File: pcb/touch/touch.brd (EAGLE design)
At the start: 97.8 x 36.2 mm, 22 parts, among them U1 MPR084EJ

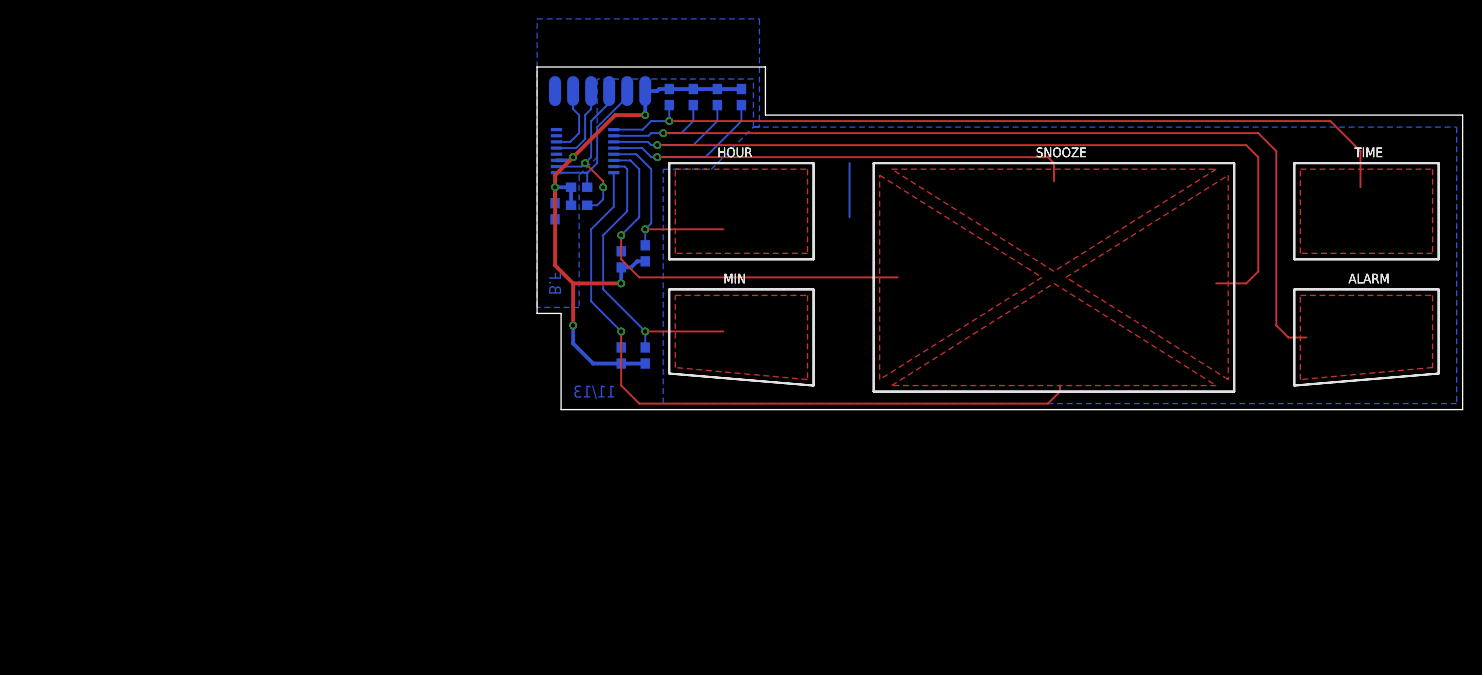
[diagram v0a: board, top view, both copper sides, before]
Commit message: Corrected drawings of touch panel PCB
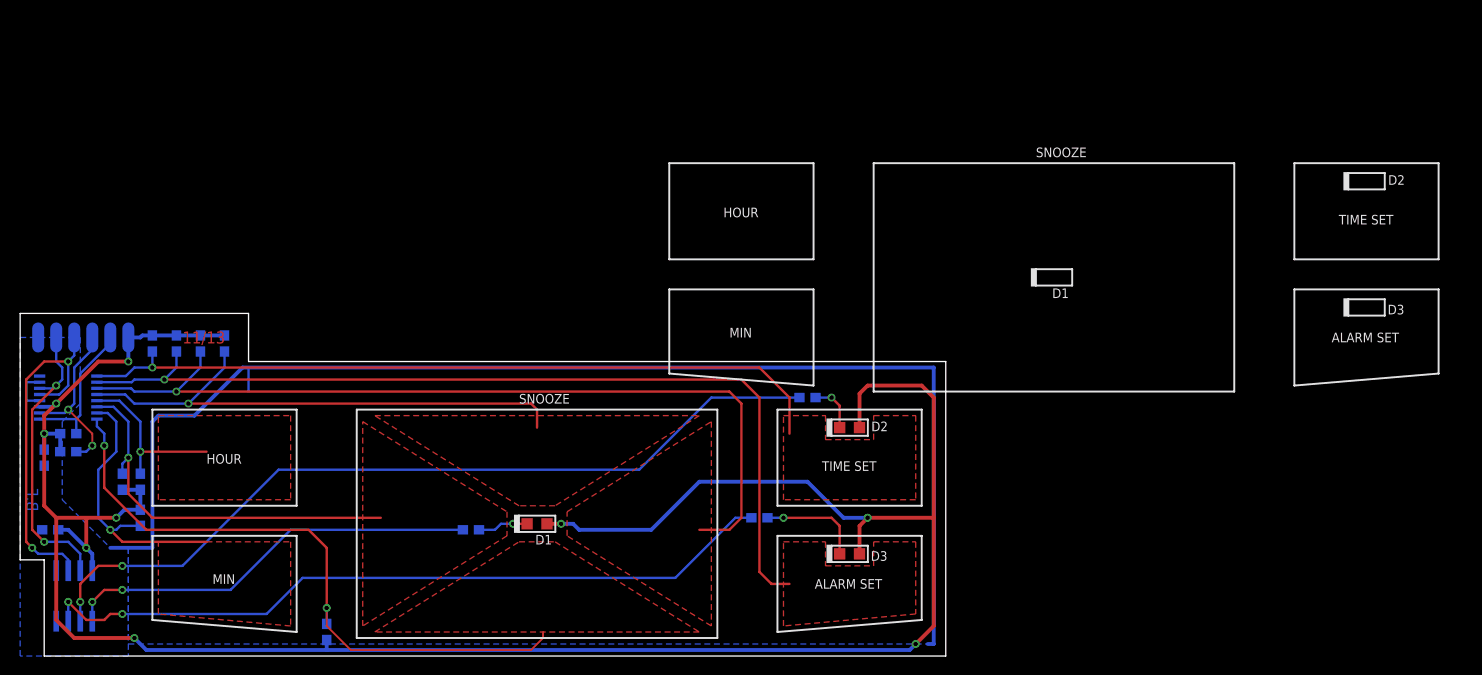
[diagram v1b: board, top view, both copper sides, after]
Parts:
- added C2: 100nF, Passive:SMD_0603
- added D1, D2, D3: {ATTR:COLOR}, Optoelectronic:CHIPLED_0805
- added R11, R12, R13: 56, Passive:SMD_0603
- added U$11, U$12, U$13, U$14, U$15, U$16: (no value), Symbols:LEGEND_ROW_30
- added U2: PCA9533D/01, IC:SOIC8
- moved !ATTN 60.5 mm to (-45.1, 7.62)
- moved !IRQ 60.5 mm to (-47.0, 7.62)
- moved 3.3V 60.5 mm to (-43.2, 7.62)
- moved R3 60.5 mm to (-35.6, 6.99)
- moved R4 60.5 mm to (-38.1, 6.99)
- moved R5 60.5 mm to (-40.6, 6.99)
- moved R7 60.5 mm to (-33.0, 6.99)
- moved SCL 60.5 mm to (-48.9, 7.62)
- moved SDA 60.5 mm to (-50.8, 7.62)
- moved U$3 60.5 mm to (-38.1, -21.0)
- moved U1 60.5 mm to (-49.5, 1.27)
- moved W6 60.5 mm to (-52.7, 7.62)
- moved C1 59.9 mm to (-52.1, -5.08)
- moved R10 59.9 mm to (-49.5, -4.45)
- moved R9 59.9 mm to (-49.5, -2.54)
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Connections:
- new net N$1: D1.K, R11.2
- new net N$2: D2.K, R12.2
- new net N$3: D3.K, R13.2
- new net N$4: R11.1, U2.1
- new net N$5: R12.1, U2.2
- new net N$6: R13.1, U2.3
- net 3.3V: now also C2.1, D1.A, D2.A, D3.A, U2.8
- net GND: now also C2.2, U2.4
- net SCL: now also U2.6
- net SDA: now also U2.7
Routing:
- net 3.3V: track 68.8 -> 257.7 mm, vias 5 -> 9
- net GND: track 5.71 -> 139.9 mm
- net N$5: track 0.00 -> 88.1 mm, vias 0 -> 2
- net N$6: track 0.00 -> 79.5 mm, vias 0 -> 2
- net N$4: track 0.00 -> 44.3 mm, vias 0 -> 2
- net SCL: track 8.76 -> 37.5 mm, vias 0 -> 2
- net SDA: track 7.48 -> 31.7 mm, vias 0 -> 2
- net N$3: track 0.00 -> 10.9 mm, vias 0 -> 1
- net E_DOWN: track 74.8 -> 68.7 mm, vias 1 -> 2
- net E_TIME: track 86.1 -> 80.4 mm
- net N$1: track 0.00 -> 5.35 mm, vias 0 -> 1
- net N$2: track 0.00 -> 5.22 mm, vias 0 -> 1
- net E_UP: track 61.2 -> 56.1 mm
- net E_RIGHT: track 94.9 -> 91.1 mm
- net E_LEFT: track 45.1 -> 41.3 mm
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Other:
- board text added: "2"
- board text added: "3"
- board text added: "3.3V"
- board text added: "4"
- board text added: "5"
- board text added: "ALARM SET"
- board text added: "ATTN"
- board text added: "C2"
- board text added: "D1"
- board text added: "D2"
- board text added: "D3"
- board text added: "GND"
- board text added: "IRQ"
- board text added: "R11"
- board text added: "R12"
- board text added: "R13"
- board text added: "SCL"
- board text added: "SDA"
- board text added: "TIME SET"
- board text added: "U2"
- board text removed: "ALARM"
- board text removed: "TIME"
